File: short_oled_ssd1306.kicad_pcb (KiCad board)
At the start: 2 copper layers, 23.5 x 19 mm, 13 parts, among them P1 n.a.

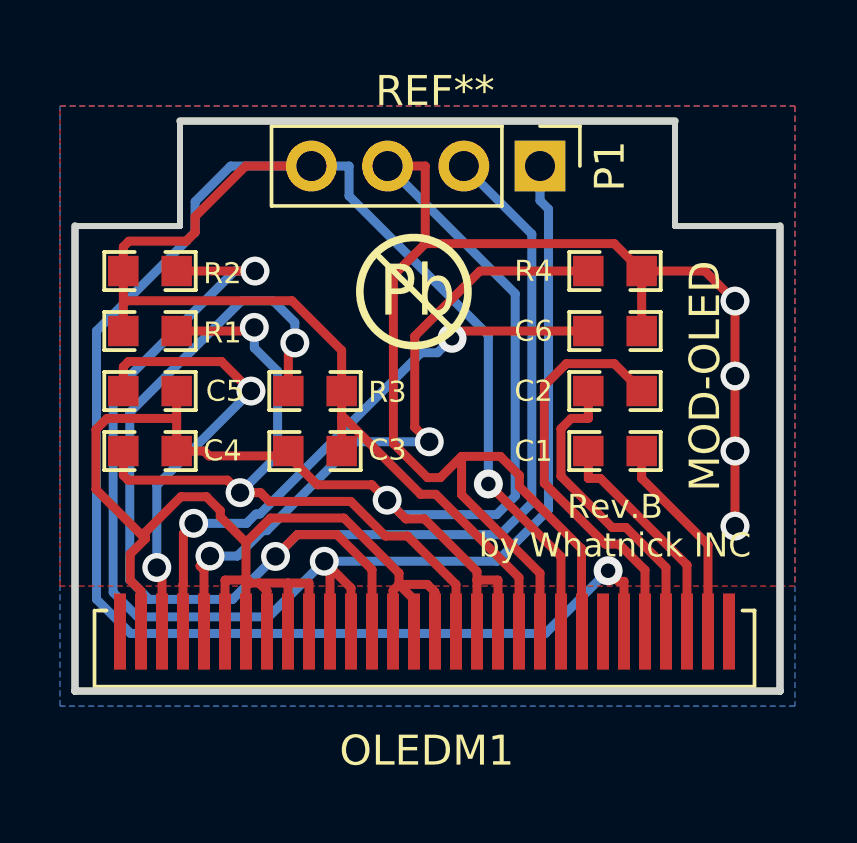
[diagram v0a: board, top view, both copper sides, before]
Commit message: Add tags to pins
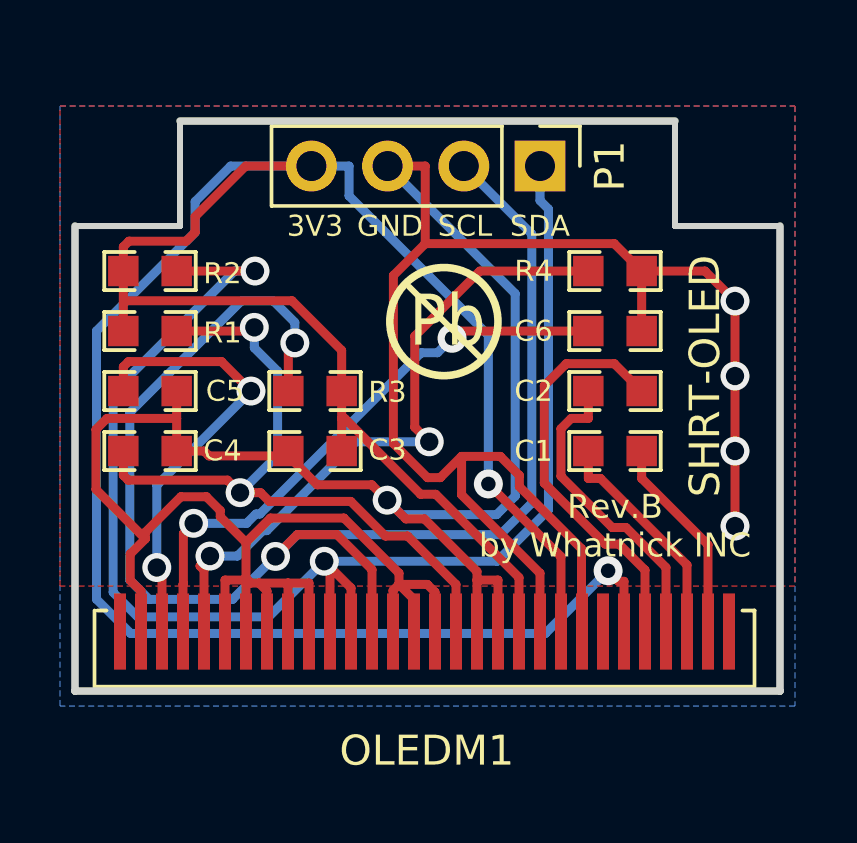
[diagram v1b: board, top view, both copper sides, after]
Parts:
- moved REF** 1.41 mm to (192.0, 134.5)
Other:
- board text added: "3V3"
- board text added: "GND"
- board text added: "SCL"
- board text added: "SDA"
- board text added: "SHRT-OLED"
- board text removed: "MOD-OLED"
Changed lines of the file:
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@@
   (general
     (thickness 1.6)
-    (drawings 12)
+    (drawings 20)
     (tracks 246)
     (zones 0)
@@
   )
   (module OLIMEX_LOGOs-FP:LOGO_PBFREE locked (layer F.Cu)
-    (at 191 133.5)
-    (fp_text reference REF** (at 0.5 -7) (layer F.SilkS)
+    (at 192 134.5)
+    (fp_text reference REF** (at 0.5 -7) (layer F.Fab)
       (effects (font (size 1 1) (thickness 0.15)))
     )
@@
     (fp_line (start -1.36398 -1.47828) (end 1.06934 0.94234) (layer F.SilkS) (width 0.2))
     (fp_circle (center -0.2032 -0.31496) (end 0.90678 -1.73482) (layer F.SilkS) (width 0.254))
+  )
+  (gr_text SDA (at 195 131) (layer B.SilkS)
+    (effects (font (size 0.7 0.7) (thickness 0.175)) (justify mirror))
+  )
+  (gr_text SCL (at 192.5 131) (layer B.SilkS)
+    (effects (font (size 0.7 0.7) (thickness 0.175)) (justify mirror))
+  )
+  (gr_text GND (at 190 131) (layer B.SilkS)
+    (effects (font (size 0.7 0.7) (thickness 0.175)) (justify mirror))
+  )
+  (gr_text 3V3 (at 187.5 131) (layer B.SilkS)
+    (effects (font (size 0.7 0.7) (thickness 0.175)) (justify mirror))
+  )
+  (gr_text SDA (at 195 131) (layer F.SilkS)
+    (effects (font (size 0.7 0.7) (thickness 0.175)))
+  )
+  (gr_text SCL (at 192.5 131) (layer F.SilkS)
+    (effects (font (size 0.7 0.7) (thickness 0.175)))
+  )
+  (gr_text GND (at 190 131) (layer F.SilkS)
+    (effects (font (size 0.7 0.7) (thickness 0.175)))
+  )
+  (gr_text 3V3 (at 187.5 131) (layer F.SilkS)
+    (effects (font (size 0.7 0.7) (thickness 0.175)))
   )
   (gr_line (start 199.5 131) (end 203 131) (layer Edge.Cuts) (width 0.2))
@@
     (effects (font (size 0.8 0.8) (thickness 0.2)))
   )
-  (gr_text MOD-OLED (at 200.5 136 90) (layer F.SilkS)
+  (gr_text SHRT-OLED (at 200.5 136 90) (layer F.SilkS)
     (effects (font (size 1.016 1.016) (thickness 0.2)))
   )
